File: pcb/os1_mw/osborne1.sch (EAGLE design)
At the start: 2 parts

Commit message: added docs
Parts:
- added JP1, JP2, JP3: (no value), pinhead:PINHD-1X4/90
- added U$3: VH396_3P, 396_conn:VH396_3P
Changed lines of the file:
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@@
 <part name="U$1" library="apricot" deviceset="MEANWELL_RD50" device=""/>
 <part name="U$2" library="os1" deviceset="TERM9.5" device=""/>
+<part name="U$3" library="396_conn" deviceset="VH396_3P" device=""/>
+<part name="JP2" library="pinhead" library_urn="urn:adsk.eagle:library:325" deviceset="PINHD-1X4" device="/90" package3d_urn="urn:adsk.eagle:package:22404/2"/>
+<part name="P+4" library="supply1" library_urn="urn:adsk.eagle:library:371" deviceset="+12V" device=""/>
+<part name="GND17" library="supply1" library_urn="urn:adsk.eagle:library:371" deviceset="GND" device=""/>
+<part name="JP1" library="pinhead" library_urn="urn:adsk.eagle:library:325" deviceset="PINHD-1X4" device="/90" package3d_urn="urn:adsk.eagle:package:22404/2"/>
+<part name="JP3" library="pinhead" library_urn="urn:adsk.eagle:library:325" deviceset="PINHD-1X4" device="/90" package3d_urn="urn:adsk.eagle:package:22404/2"/>
 </parts>
 <sheets>
@@
 <instance part="U$1" gate="G$1" x="45.72" y="38.1" smashed="yes"/>
 <instance part="U$2" gate="G$1" x="109.22" y="43.18" smashed="yes"/>
+<instance part="U$3" gate="G$1" x="111.76" y="-7.62" smashed="yes"/>
+<instance part="JP2" gate="A" x="175.26" y="73.66" smashed="yes">
+<attribute name="NAME" x="168.91" y="81.915" size="1.778" layer="95"/>
+<attribute name="VALUE" x="168.91" y="66.04" size="1.778" layer="96"/>
+</instance>
+<instance part="P+4" gate="1" x="185.42" y="76.2" smashed="yes" rot="MR0">
+<attribute name="VALUE" x="187.96" y="71.12" size="1.778" layer="96" rot="MR90"/>
+</instance>
+<instance part="GND17" gate="1" x="162.56" y="68.58" smashed="yes">
+<attribute name="VALUE" x="160.02" y="66.04" size="1.778" layer="96"/>
+</instance>
+<instance part="JP1" gate="A" x="175.26" y="99.06" smashed="yes">
+<attribute name="NAME" x="168.91" y="107.315" size="1.778" layer="95"/>
+<attribute name="VALUE" x="168.91" y="91.44" size="1.778" layer="96"/>
+</instance>
+<instance part="JP3" gate="A" x="175.26" y="119.38" smashed="yes">
+<attribute name="NAME" x="168.91" y="127.635" size="1.778" layer="95"/>
+<attribute name="VALUE" x="168.91" y="111.76" size="1.778" layer="96"/>
+</instance>
 </instances>
 <busses>
@@
 which will not be processed correctly with this version.
 </note>
+<note version="8.2" severity="warning">
+Since Version 8.2, EAGLE supports online libraries. The ids
+of those online libraries will not be understood (or retained)
+with this version.
+</note>
+<note version="8.3" severity="warning">
+Since Version 8.3, EAGLE supports URNs for individual library
+assets (packages, symbols, and devices). The URNs of those assets
+will not be understood (or retained) with this version.
+</note>
+<note version="8.3" severity="warning">
+Since Version 8.3, EAGLE supports the association of 3D packages
+with devices in libraries, schematics, and board files. Those 3D
+packages will not be understood (or retained) with this version.
+</note>
 </compatibility>

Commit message: new os1 pcb done
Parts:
- removed U$3: VH396_3P, 396_conn:VH396_3P
- added C4, C6: (no value), capacitor-wima:C5/2.5
- added C5: (no value), adafruit_changed:CPOL-USE3.5-8
- added JP4: (no value), appleii:4PIN_FAN
- added TP1, TP2: PTR1PAD1-17, testpad:PTR1PAD1-17
- added U$4, U$5, U$6, U$8: M3_HOLE_PLATED, os1:M3_HOLE_PLATED
- added U$7: 396_2P_LIVE, 396_conn:396_2P_LIVE
- added U$9: CAR_FUSE_HOLDER3IN1, atx_power_control:CAR_FUSE_HOLDER3IN1
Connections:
- new net +12V: JP1.2, JP2.2, JP3.2, JP4.2_VCC, U$2.P$3
- new net +5V: C4.1, C5.+, C6.1, JP1.4, JP2.4, JP3.4, U$9.A0, U$9.A1
- new net GND: C4.2, C5.-, C6.2, JP1.3, JP2.3, JP3.3, JP4.1_GND, TP1.TP, TP2.TP, U$2.P$2, U$2.P$4, U$2.P$5, U$4.P$1, U$5.P$1, U$6.P$1, U$8.P$1
- new net LIVE: U$2.P$7, U$7.P$1
- new net N$2: U$2.P$1, U$9.B0, U$9.B1
- new net NEUTRAL: U$2.P$6, U$7.P$2
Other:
- moved on the sheet: JP1, JP2, JP3

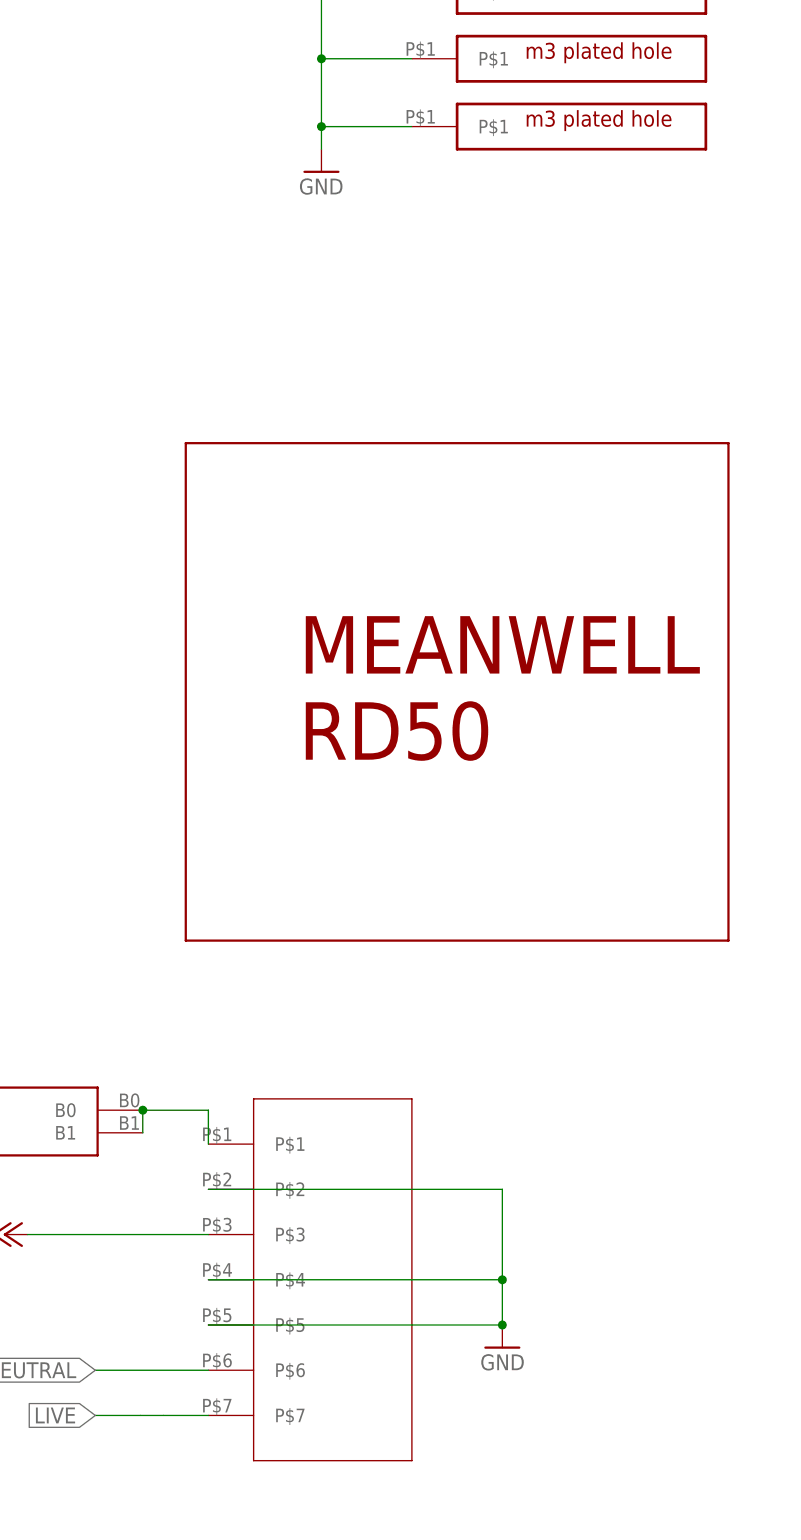
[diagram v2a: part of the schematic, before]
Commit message: isolated pe and gnd
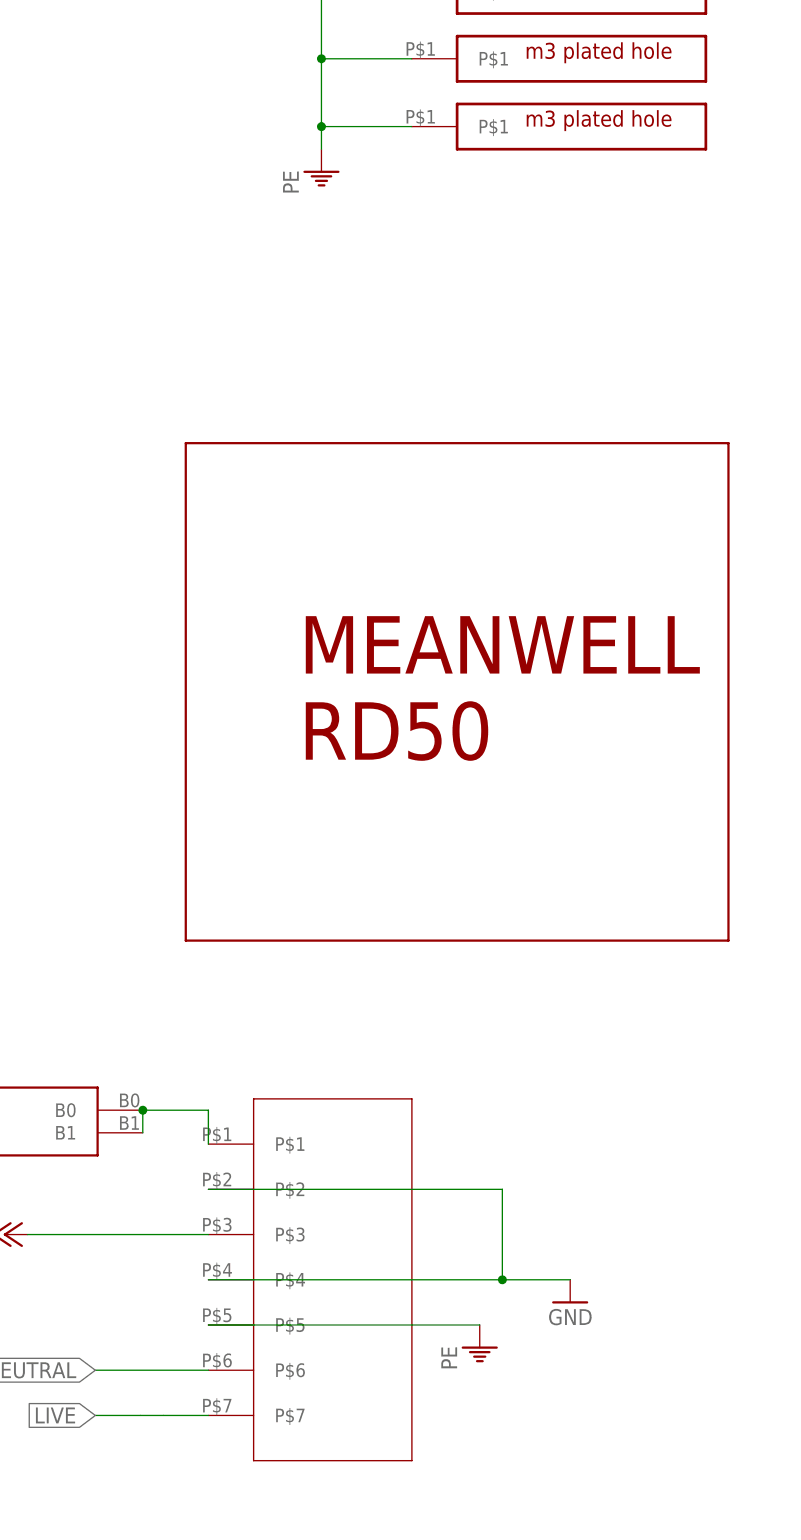
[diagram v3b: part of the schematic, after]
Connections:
- new net PE: U$2.P$5, U$4.P$1, U$5.P$1, U$6.P$1, U$8.P$1
- net GND: no longer U$2.P$5, U$4.P$1, U$5.P$1, U$6.P$1, U$8.P$1
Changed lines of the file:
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@@
 <part name="U$6" library="os1" deviceset="M3_HOLE_PLATED" device=""/>
 <part name="U$8" library="os1" deviceset="M3_HOLE_PLATED" device=""/>
-<part name="GND1" library="supply1" library_urn="urn:adsk.eagle:library:371" deviceset="GND" device=""/>
 <part name="U$9" library="atx_power_control" deviceset="CAR_FUSE_HOLDER" device="3IN1"/>
 <part name="C4" library="capacitor-wima" library_urn="urn:adsk.eagle:library:116" deviceset="C" device="5/2.5" package3d_urn="urn:adsk.eagle:package:5426/1"/>
@@
 <part name="GND13" library="supply1" library_urn="urn:adsk.eagle:library:371" deviceset="GND" device=""/>
 <part name="P+10" library="supply1" library_urn="urn:adsk.eagle:library:371" deviceset="+12V" device=""/>
+<part name="PE1" library="supply1" library_urn="urn:adsk.eagle:library:371" deviceset="PE" device=""/>
+<part name="PE2" library="supply1" library_urn="urn:adsk.eagle:library:371" deviceset="PE" device=""/>
 </parts>
 <sheets>
@@
 <instance part="U$6" gate="G$1" x="53.34" y="99.06" smashed="yes"/>
 <instance part="U$8" gate="G$1" x="53.34" y="121.92" smashed="yes"/>
-<instance part="GND1" gate="1" x="27.94" y="96.52" smashed="yes">
-<attribute name="VALUE" x="25.4" y="93.98" size="1.778" layer="96"/>
-</instance>
 <instance part="U$9" gate="G$1" x="-7.62" y="-10.16" smashed="yes"/>
 <instance part="C4" gate="G$1" x="-43.18" y="-15.24" smashed="yes">
@@
 <attribute name="VALUE" x="-10.16" y="-22.86" size="1.778" layer="96" rot="MR0"/>
 </instance>
-<instance part="GND4" gate="1" x="48.26" y="-35.56" smashed="yes" rot="MR0">
-<attribute name="VALUE" x="50.8" y="-38.1" size="1.778" layer="96" rot="MR0"/>
+<instance part="GND4" gate="1" x="55.88" y="-30.48" smashed="yes" rot="MR0">
+<attribute name="VALUE" x="58.42" y="-33.02" size="1.778" layer="96" rot="MR0"/>
 </instance>
 <instance part="U$7" gate="G$1" x="10.16" y="-68.58" smashed="yes" rot="R180"/>
@@
 <instance part="P+10" gate="1" x="200.66" y="25.4" smashed="yes" rot="MR0">
 <attribute name="VALUE" x="203.2" y="20.32" size="1.778" layer="96" rot="MR90"/>
+</instance>
+<instance part="PE1" gate="M" x="45.72" y="-35.56" smashed="yes">
+<attribute name="VALUE" x="43.18" y="-38.1" size="1.778" layer="96" rot="R90"/>
+</instance>
+<instance part="PE2" gate="M" x="27.94" y="96.52" smashed="yes">
+<attribute name="VALUE" x="25.4" y="93.98" size="1.778" layer="96" rot="R90"/>
 </instance>
 </instances>
@@
 <net name="GND" class="0">
 <segment>
-<pinref part="U$8" gate="G$1" pin="P$1"/>
-<pinref part="GND1" gate="1" pin="GND"/>
-<wire x1="38.1" y1="124.46" x2="27.94" y2="124.46" width="0.1524" layer="91"/>
-<wire x1="27.94" y1="124.46" x2="27.94" y2="116.84" width="0.1524" layer="91"/>
-<pinref part="U$6" gate="G$1" pin="P$1"/>
-<wire x1="27.94" y1="116.84" x2="27.94" y2="109.22" width="0.1524" layer="91"/>
-<wire x1="27.94" y1="109.22" x2="27.94" y2="101.6" width="0.1524" layer="91"/>
-<wire x1="27.94" y1="101.6" x2="27.94" y2="99.06" width="0.1524" layer="91"/>
-<wire x1="38.1" y1="101.6" x2="27.94" y2="101.6" width="0.1524" layer="91"/>
-<junction x="27.94" y="101.6"/>
-<pinref part="U$4" gate="G$1" pin="P$1"/>
-<wire x1="38.1" y1="116.84" x2="27.94" y2="116.84" width="0.1524" layer="91"/>
-<junction x="27.94" y="116.84"/>
-<pinref part="U$5" gate="G$1" pin="P$1"/>
-<wire x1="38.1" y1="109.22" x2="27.94" y2="109.22" width="0.1524" layer="91"/>
-<junction x="27.94" y="109.22"/>
-</segment>
-<segment>
 <pinref part="C6" gate="G$1" pin="2"/>
 <pinref part="GND10" gate="1" pin="GND"/>
@@
 </segment>
 <segment>
-<pinref part="U$2" gate="G$1" pin="P$5"/>
 <pinref part="GND4" gate="1" pin="GND"/>
-<wire x1="15.24" y1="-33.02" x2="48.26" y2="-33.02" width="0.1524" layer="91"/>
 <pinref part="U$2" gate="G$1" pin="P$4"/>
 <wire x1="15.24" y1="-27.94" x2="48.26" y2="-27.94" width="0.1524" layer="91"/>
-<wire x1="48.26" y1="-27.94" x2="48.26" y2="-33.02" width="0.1524" layer="91"/>
-<junction x="48.26" y="-33.02"/>
+<wire x1="48.26" y1="-27.94" x2="55.88" y2="-27.94" width="0.1524" layer="91"/>
 <pinref part="U$2" gate="G$1" pin="P$2"/>
 <wire x1="15.24" y1="-17.78" x2="48.26" y2="-17.78" width="0.1524" layer="91"/>
@@
 </segment>
 </net>
+<net name="PE" class="0">
+<segment>
+<pinref part="U$2" gate="G$1" pin="P$5"/>
+<pinref part="PE1" gate="M" pin="PE"/>
+<wire x1="15.24" y1="-33.02" x2="45.72" y2="-33.02" width="0.1524" layer="91"/>
+</segment>
+<segment>
+<pinref part="U$8" gate="G$1" pin="P$1"/>
+<wire x1="38.1" y1="124.46" x2="27.94" y2="124.46" width="0.1524" layer="91"/>
+<wire x1="27.94" y1="124.46" x2="27.94" y2="116.84" width="0.1524" layer="91"/>
+<pinref part="U$6" gate="G$1" pin="P$1"/>
+<wire x1="27.94" y1="116.84" x2="27.94" y2="109.22" width="0.1524" layer="91"/>
+<wire x1="27.94" y1="109.22" x2="27.94" y2="101.6" width="0.1524" layer="91"/>
+<wire x1="27.94" y1="101.6" x2="27.94" y2="99.06" width="0.1524" layer="91"/>
+<wire x1="38.1" y1="101.6" x2="27.94" y2="101.6" width="0.1524" layer="91"/>
+<junction x="27.94" y="101.6"/>
+<pinref part="U$4" gate="G$1" pin="P$1"/>
+<wire x1="38.1" y1="116.84" x2="27.94" y2="116.84" width="0.1524" layer="91"/>
+<junction x="27.94" y="116.84"/>
+<pinref part="U$5" gate="G$1" pin="P$1"/>
+<wire x1="38.1" y1="109.22" x2="27.94" y2="109.22" width="0.1524" layer="91"/>
+<junction x="27.94" y="109.22"/>
+<pinref part="PE2" gate="M" pin="PE"/>
+</segment>
+</net>
